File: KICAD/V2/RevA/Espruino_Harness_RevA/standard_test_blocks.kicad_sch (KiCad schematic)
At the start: 97 parts, among them J201 EXTERNAL_ANALOG_STIMULUS_0_TO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, J301 GROVE_I2C, J302 MCP23017_GPIO, J401 MCP3008_ANALOGUE_BREAKOUT, J402 ADAFRUIT_MICROSD_BFF_5683, J501 DS18B20_SENSOR_A, J502 DS18B20_SENSOR_B, J503 2K2_DQ_4K7, J504 DS2413_MODULE, J701 UART_PEER_DIAGNOSTIC, J902 PIXEL_SHIFTER_6066, Q301 2N7002, Q302 2N7002, U301 MCP23017-E/SO, U401 MCP3008, U701 TMUX1511

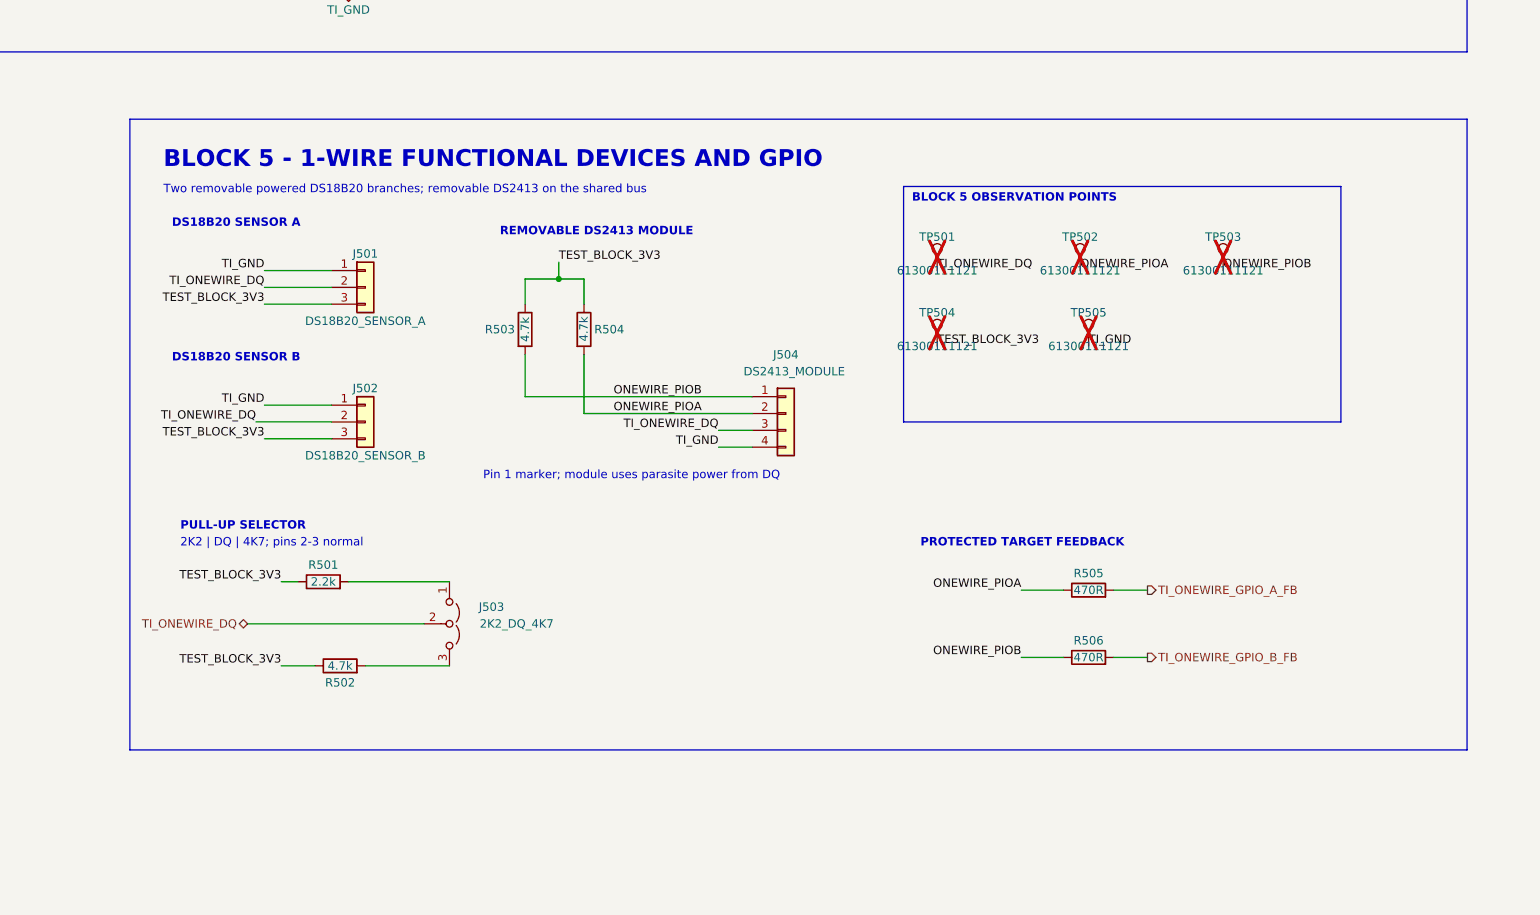
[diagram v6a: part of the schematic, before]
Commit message: Verify TB05 OneWire functional-device baseline
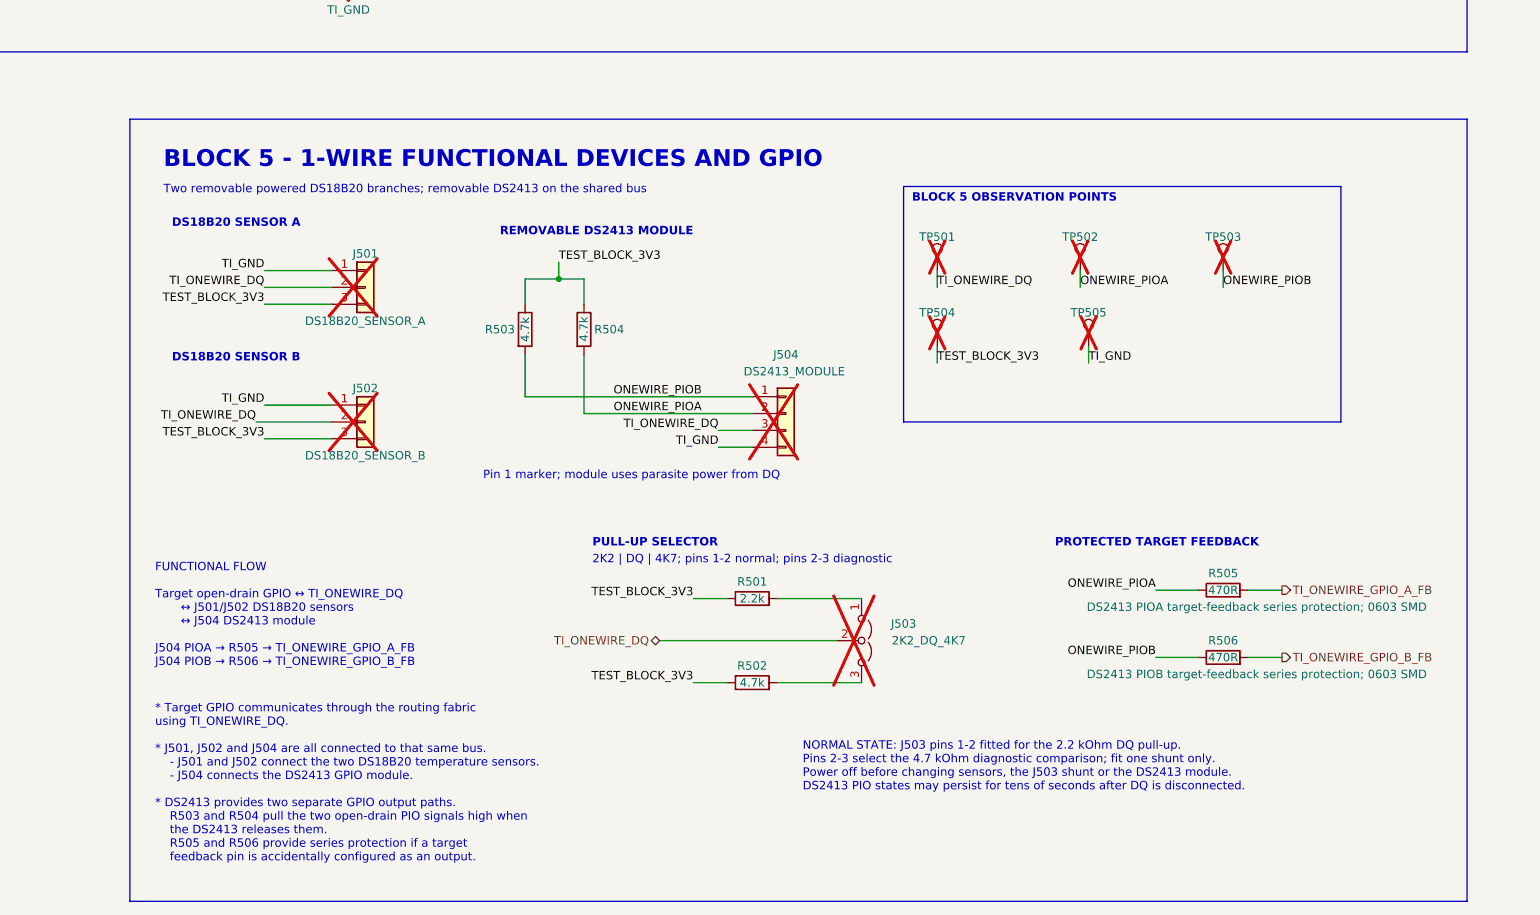
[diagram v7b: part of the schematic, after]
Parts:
- J501, J502: MPN (none) -> 1725669; now not fitted
- J503: MPN (none) -> 61300311121; SHUNT_MPN (none) -> 60900213421; now not fitted; now in the parts list
- J504: MPN (none) -> 61300411121; now not fitted
- R501: AISLER_MPN (none) -> 2.2k 0603 1% 0.1W
- R502, R503, R504: AISLER_MPN (none) -> 4.7k 0603 1% 0.1W
- R505, R506: AISLER_MPN (none) -> 470R 0603 1% 0.1W
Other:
- note added: "* Target GPIO communicates through the routing fabric using TI_ONEWIRE_DQ. * J501, J502 and J504 are all connected to that same bus. - J501 and J502 connect the two DS18B20 temperature sensors. - J504 connects the DS2413 GPIO module. * DS2413 provides two separate GPIO output paths. R503 and R504 pull the two open-drain PIO signals high when the DS2413 releases them. R505 and R506 provide series 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"
- note added: "2K2 | DQ | 4K7; pins 1-2 normal; pins 2-3 diagnostic"
- note added: "FUNCTIONAL FLOW Target open-drain GPIO ↔ TI_ONEWIRE_DQ ↔ J501/J502 DS18B20 sensors ↔ J504 DS2413 module J504 PIOA → R505 → TI_ONEWIRE_GPIO_A_FB J504 PIOB → R506 → TI_ONEWIRE_GPIO_B_FB"
- note added: "NORMAL STATE: J503 pins 1-2 fitted for the 2.2 kOhm DQ pull-up. Pins 2-3 select the 4.7 kOhm diagnostic comparison; fit one shunt only. Power off before changing sensors, the J503 shunt or the DS2413 module. DS2413 PIO states may persist for tens of seconds after DQ is disconnected."
- note removed: "2K2 | DQ | 4K7; pins 2-3 normal"
- moved on the sheet: R501, R502, R505, R506

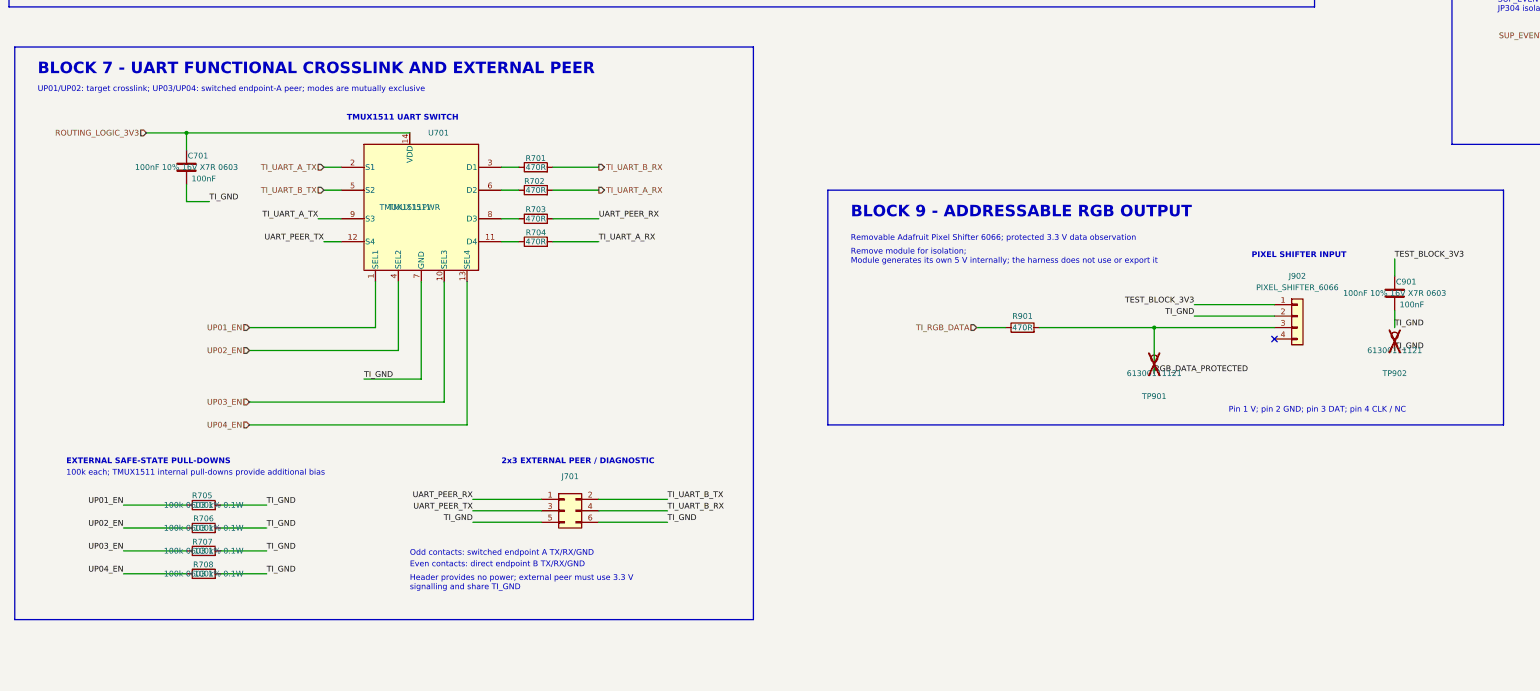
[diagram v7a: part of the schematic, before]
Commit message: Verify TB07 UART crosslink baseline
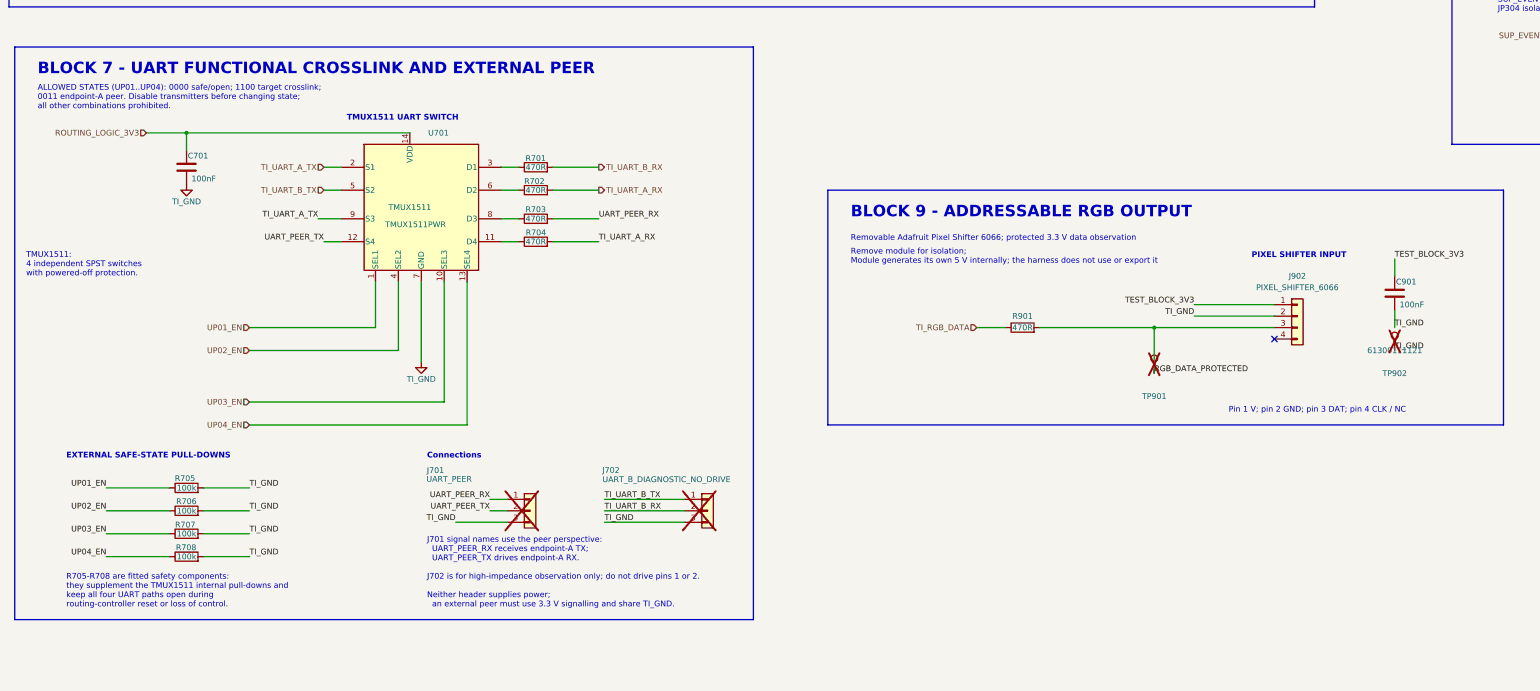
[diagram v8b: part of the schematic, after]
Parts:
- removed J701: UART_PEER_DIAGNOSTIC, Connector_PinHeader_2.54mm:PinHeader_2x03_P2.54mm_Vertical, symbol Connector_Generic:Conn_02x03_Odd_Even
- added J701: UART_PEER, Connector_PinHeader_2.54mm:PinHeader_1x03_P2.54mm_Vertical, symbol Connector_Generic:Conn_01x03
- added J702: UART_B_DIAGNOSTIC_NO_DRIVE, Connector_PinHeader_2.54mm:PinHeader_1x03_P2.54mm_Vertical, symbol Connector_Generic:Conn_01x03
- R701, R702, R703, R704: AISLER_MPN (none) -> 470R 0603 1% 0.1W
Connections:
- net TI_GND: now also J701.3 (Pin_3), J702.3 (Pin_3)
- net TI_UART_B_RX: now also J702.2 (Pin_2)
- net TI_UART_B_TX: now also J702.1 (Pin_1)
- net UART_PEER_RX: now also J701.1 (Pin_1)
- net UART_PEER_TX: now also J701.2 (Pin_2)
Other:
- note added: "ALLOWED STATES (UP01..UP04): 0000 safe/open; 1100 target crosslink; 0011 endpoint-A peer. Disable transmitters before changing state; all other combinations prohibited."
- note added: "Connections"
- note added: "J701 signal names use the peer perspective: UART_PEER_RX receives endpoint-A TX; UART_PEER_TX drives endpoint-A RX. J702 is for high-impedance observation only; do not drive pins 1 or 2. Neither header supplies power; an external peer must use 3.3 V signalling and share TI_GND."
- note added: "R705-R708 are fitted safety components: they supplement the TMUX1511 internal pull-downs and keep all four UART paths open during routing-controller reset or loss of control."
- note added: "TMUX1511: 4 independent SPST switches with powered-off protection."
- note removed: "100k each; TMUX1511 internal pull-downs provide additional bias"
- note removed: "2x3 EXTERNAL PEER / DIAGNOSTIC"
- note removed: "Even contacts: direct endpoint B TX/RX/GND"
- note removed: "Header provides no power; external peer must use 3.3 V signalling and share TI_GND"
- note removed: "Odd contacts: switched endpoint A TX/RX/GND"
- note removed: "UP01/UP02: target crosslink; UP03/UP04: switched endpoint-A peer; modes are mutually exclusive"
- moved on the sheet: R705, R706, R707, R708
